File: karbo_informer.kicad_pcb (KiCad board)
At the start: 2 copper layers, 12 parts, among them IC1 MAX7219, IC2 MAX7219, P1 USB_OTG

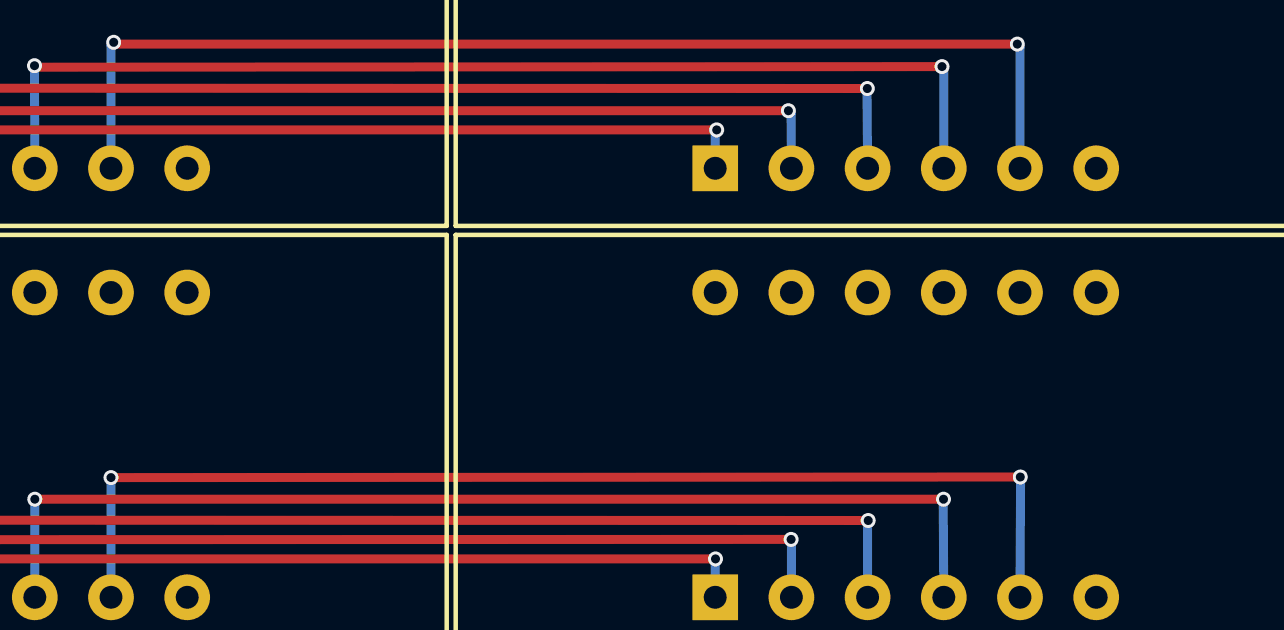
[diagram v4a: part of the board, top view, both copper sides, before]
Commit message: Wire for segments B in the sell line (D2 to D4)
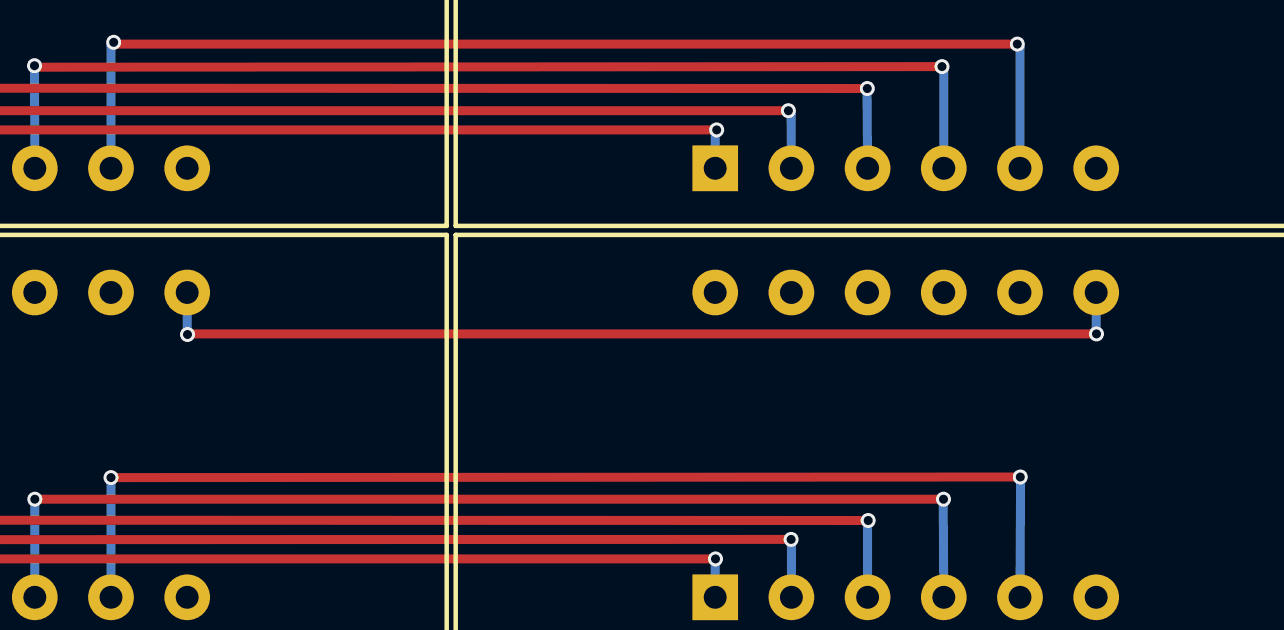
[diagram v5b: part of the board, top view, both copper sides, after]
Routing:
- net /S_SEG_B: track 0.00 -> 33.0 mm, vias 0 -> 2
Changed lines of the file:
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@@
   (general
     (links 69)
-    (no_connects 56)
+    (no_connects 55)
     (area 0 0 0 0)
     (thickness 1.6)
     (drawings 0)
-    (tracks 90)
+    (tracks 95)
     (zones 0)
     (modules 12)
@@
   (segment (start 44.62 44.29) (end 74.92 44.27) (width 0.3) (layer F.Cu) (net 17))
   (via (at 44.61 44.29) (size 0.5) (drill 0.3) (layers F.Cu B.Cu) (net 17))
+  (segment (start 47.15 38.12) (end 47.15 39.51) (width 0.3) (layer B.Cu) (net 24) (status 400000))
+  (segment (start 77.45 39.49) (end 77.45 38.12) (width 0.3) (layer B.Cu) (net 24) (status 800000))
+  (via (at 77.46 39.5) (size 0.5) (drill 0.3) (layers F.Cu B.Cu) (net 24))
+  (segment (start 47.18 39.5) (end 77.46 39.5) (width 0.3) (layer F.Cu) (net 24))
+  (via (at 47.16 39.52) (size 0.5) (drill 0.3) (layers F.Cu B.Cu) (net 24))
 )

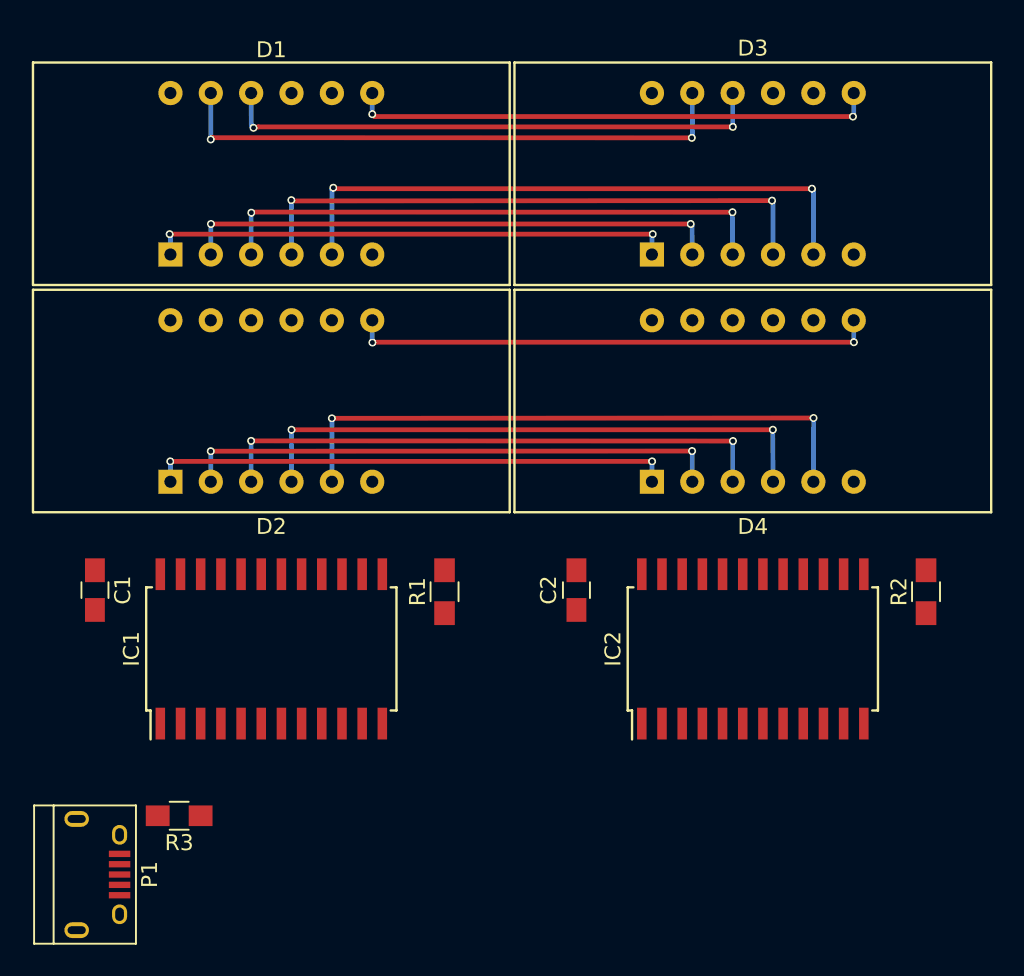
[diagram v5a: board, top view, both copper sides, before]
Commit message: Wire for DIG0 and other in the buy line
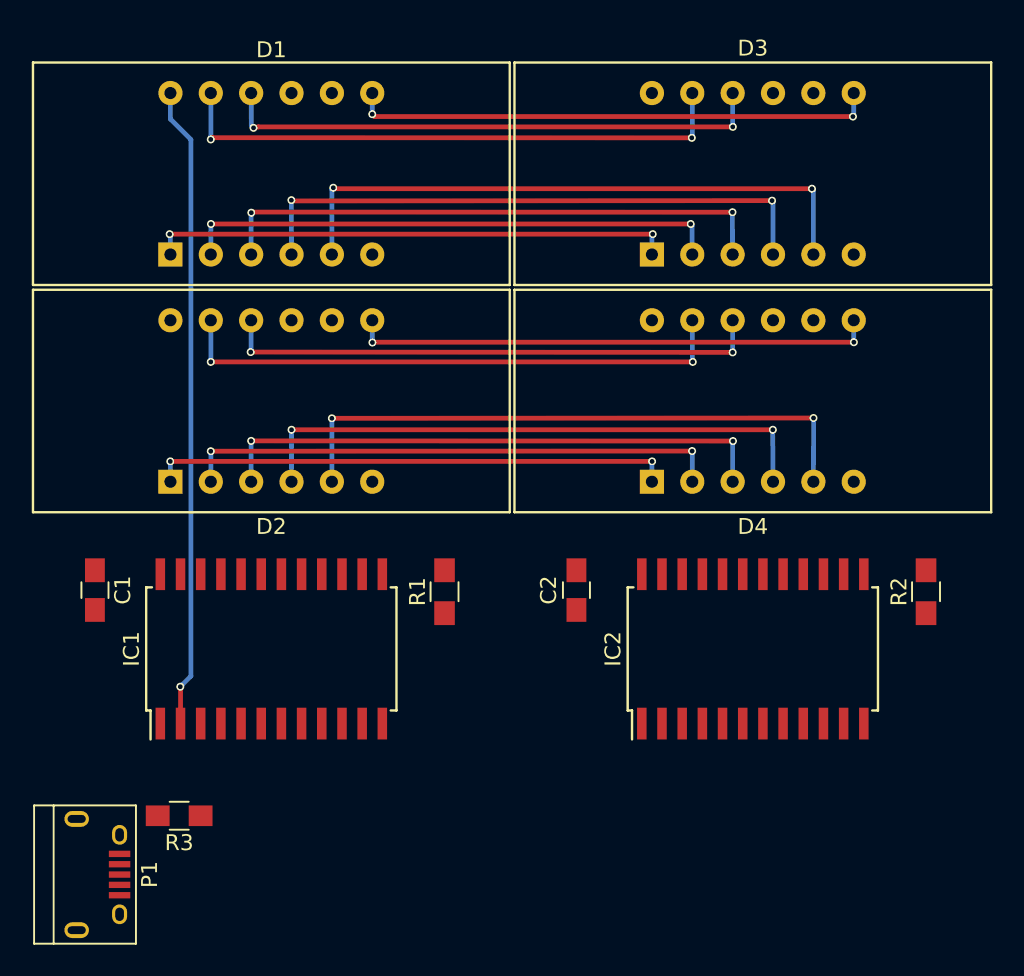
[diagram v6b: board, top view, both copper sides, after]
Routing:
- net /B_DIG_0: track 0.00 -> 40.5 mm, vias 0 -> 1
- net /S_SEG_A: track 0.00 -> 35.6 mm, vias 0 -> 2
- net /S_SEG_F: track 0.00 -> 34.3 mm, vias 0 -> 2
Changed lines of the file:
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@@
   (general
     (links 69)
-    (no_connects 55)
+    (no_connects 52)
     (area 0 0 0 0)
     (thickness 1.6)
     (drawings 0)
-    (tracks 95)
+    (tracks 112)
     (zones 0)
     (modules 12)
@@
   (segment (start 36.99 26.74) (end 37.1 26.63) (width 0.3) (layer F.Cu) (net 8))
   (via (at 36.99 26.74) (size 0.5) (drill 0.3) (layers F.Cu B.Cu) (net 8))
+  (segment (start 35.085 61.195) (end 35.085 63.5) (width 0.3) (layer F.Cu) (net 9))
+  (segment (start 35.07 61.18) (end 35.085 61.195) (width 0.3) (layer F.Cu) (net 9))
+  (via (at 35.07 61.18) (size 0.5) (drill 0.3) (layers F.Cu B.Cu) (net 9))
+  (segment (start 35.74 60.51) (end 35.07 61.18) (width 0.3) (layer B.Cu) (net 9))
+  (segment (start 35.74 26.75) (end 35.74 60.51) (width 0.3) (layer B.Cu) (net 9))
+  (segment (start 34.45 25.46) (end 35.74 26.75) (width 0.3) (layer B.Cu) (net 9))
+  (segment (start 34.45 23.82) (end 34.45 25.46) (width 0.3) (layer B.Cu) (net 9))
   (via (at 77.4 25.3) (size 0.5) (drill 0.3) (layers F.Cu B.Cu) (net 12))
   (segment (start 77.4 25.3) (end 77.45 25.3) (width 0.3) (layer B.Cu) (net 12))
@@
   (via (at 69.85 45.72) (size 0.5) (drill 0.3) (layers F.Cu B.Cu) (net 14))
   (segment (start 69.85 45.72) (end 69.83 45.74) (width 0.3) (layer B.Cu) (net 14))
-  (segment (start 69.83 48.28) (end 69.83 45.74) (width 0.3) (layer B.Cu) (net 14) (status 400000))
+  (segment (start 69.83 48.28) (end 69.83 45.74) (width 0.3) (layer B.Cu) (net 14))
   (segment (start 39.53 45.71) (end 39.53 48.3) (width 0.3) (layer B.Cu) (net 14))
   (via (at 36.99 46.36) (size 0.5) (drill 0.3) (layers F.Cu B.Cu) (net 15))
   (via (at 67.28 46.35) (size 0.5) (drill 0.3) (layers F.Cu B.Cu) (net 15))
   (segment (start 67.28 46.35) (end 36.99 46.36) (width 0.3) (layer F.Cu) (net 15))
-  (segment (start 36.99 46.36) (end 36.99 48.28) (width 0.3) (layer B.Cu) (net 15) (status 800000))
+  (segment (start 36.99 46.36) (end 36.99 48.28) (width 0.3) (layer B.Cu) (net 15))
   (segment (start 67.29 46.36) (end 67.29 48.28) (width 0.3) (layer B.Cu) (net 15))
   (via (at 42.07 45.01) (size 0.5) (drill 0.3) (layers F.Cu B.Cu) (net 16))
-  (segment (start 42.07 48.28) (end 42.07 45.01) (width 0.3) (layer B.Cu) (net 16) (status 400000))
-  (segment (start 72.35 45.02) (end 72.37 48.28) (width 0.3) (layer B.Cu) (net 16) (status 800000))
+  (segment (start 42.07 48.28) (end 42.07 45.01) (width 0.3) (layer B.Cu) (net 16))
+  (segment (start 72.35 45.02) (end 72.37 48.28) (width 0.3) (layer B.Cu) (net 16))
   (via (at 72.36 45.01) (size 0.5) (drill 0.3) (layers F.Cu B.Cu) (net 16))
   (segment (start 42.07 45.01) (end 72.36 45.01) (width 0.3) (layer F.Cu) (net 16))
-  (segment (start 44.61 48.28) (end 44.61 44.29) (width 0.3) (layer B.Cu) (net 17) (status 400000))
-  (segment (start 74.93 44.28) (end 74.91 48.28) (width 0.3) (layer B.Cu) (net 17) (status 800000))
+  (segment (start 44.61 48.28) (end 44.61 44.29) (width 0.3) (layer B.Cu) (net 17))
+  (segment (start 74.93 44.28) (end 74.91 48.28) (width 0.3) (layer B.Cu) (net 17))
   (via (at 74.92 44.27) (size 0.5) (drill 0.3) (layers F.Cu B.Cu) (net 17))
   (segment (start 44.62 44.29) (end 74.92 44.27) (width 0.3) (layer F.Cu) (net 17))
   (via (at 44.61 44.29) (size 0.5) (drill 0.3) (layers F.Cu B.Cu) (net 17))
-  (segment (start 47.15 38.12) (end 47.15 39.51) (width 0.3) (layer B.Cu) (net 24) (status 400000))
-  (segment (start 77.45 39.49) (end 77.45 38.12) (width 0.3) (layer B.Cu) (net 24) (status 800000))
+  (via (at 39.5 40.12) (size 0.5) (drill 0.3) (layers F.Cu B.Cu) (net 19))
+  (segment (start 39.5 40.12) (end 69.83 40.14) (width 0.3) (layer F.Cu) (net 19))
+  (via (at 69.83 40.14) (size 0.5) (drill 0.3) (layers F.Cu B.Cu) (net 19))
+  (segment (start 69.83 38.12) (end 69.83 40.14) (width 0.3) (layer B.Cu) (net 19))
+  (segment (start 39.53 40.09) (end 39.53 38.12) (width 0.3) (layer B.Cu) (net 19))
+  (segment (start 36.99 40.74) (end 36.99 38.12) (width 0.3) (layer B.Cu) (net 20))
+  (via (at 36.99 40.74) (size 0.5) (drill 0.3) (layers F.Cu B.Cu) (net 20))
+  (segment (start 67.29 38.12) (end 67.3 40.72) (width 0.3) (layer B.Cu) (net 20))
+  (via (at 67.32 40.74) (size 0.5) (drill 0.3) (layers F.Cu B.Cu) (net 20))
+  (segment (start 36.99 40.74) (end 67.32 40.74) (width 0.3) (layer F.Cu) (net 20))
+  (segment (start 47.15 38.12) (end 47.15 39.51) (width 0.3) (layer B.Cu) (net 24))
+  (segment (start 77.45 39.49) (end 77.45 38.12) (width 0.3) (layer B.Cu) (net 24))
   (via (at 77.46 39.5) (size 0.5) (drill 0.3) (layers F.Cu B.Cu) (net 24))
   (segment (start 47.18 39.5) (end 77.46 39.5) (width 0.3) (layer F.Cu) (net 24))

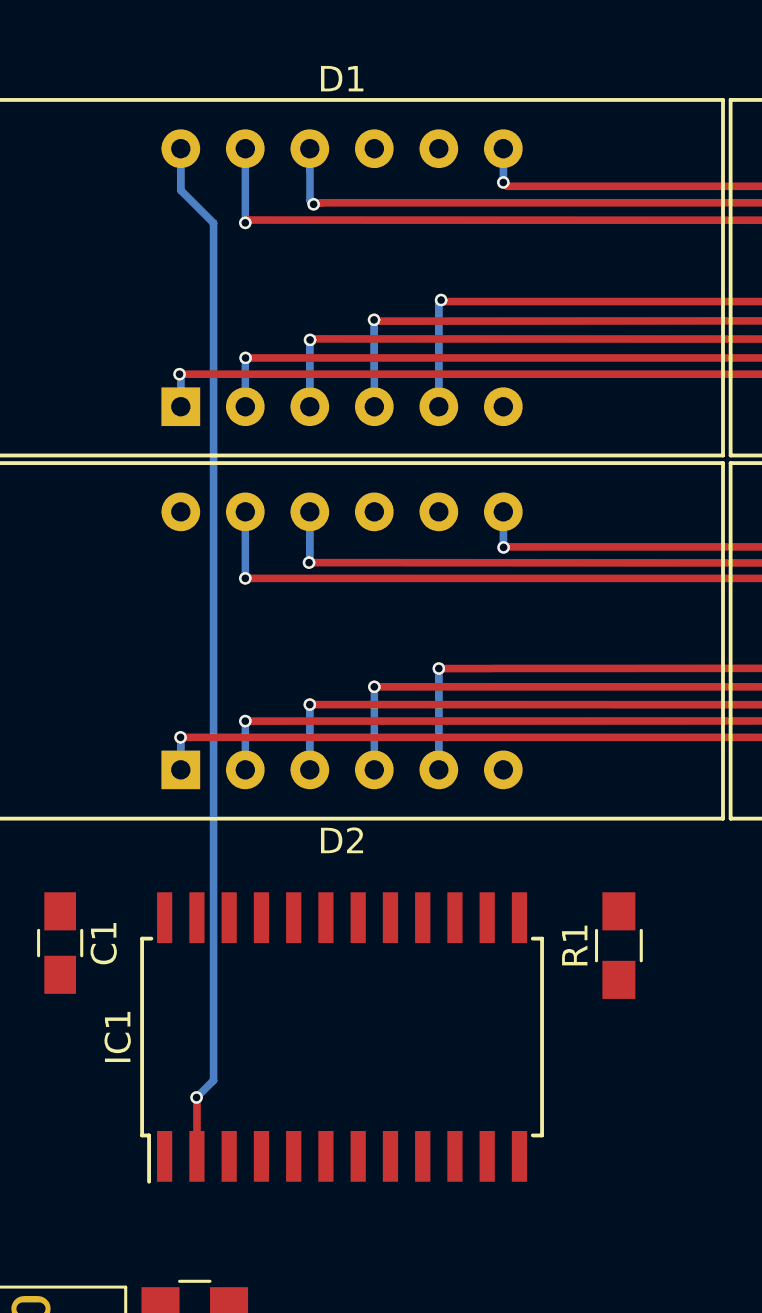
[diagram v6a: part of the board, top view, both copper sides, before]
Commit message: Wire for DIG2 to MAX7219 in the buy line
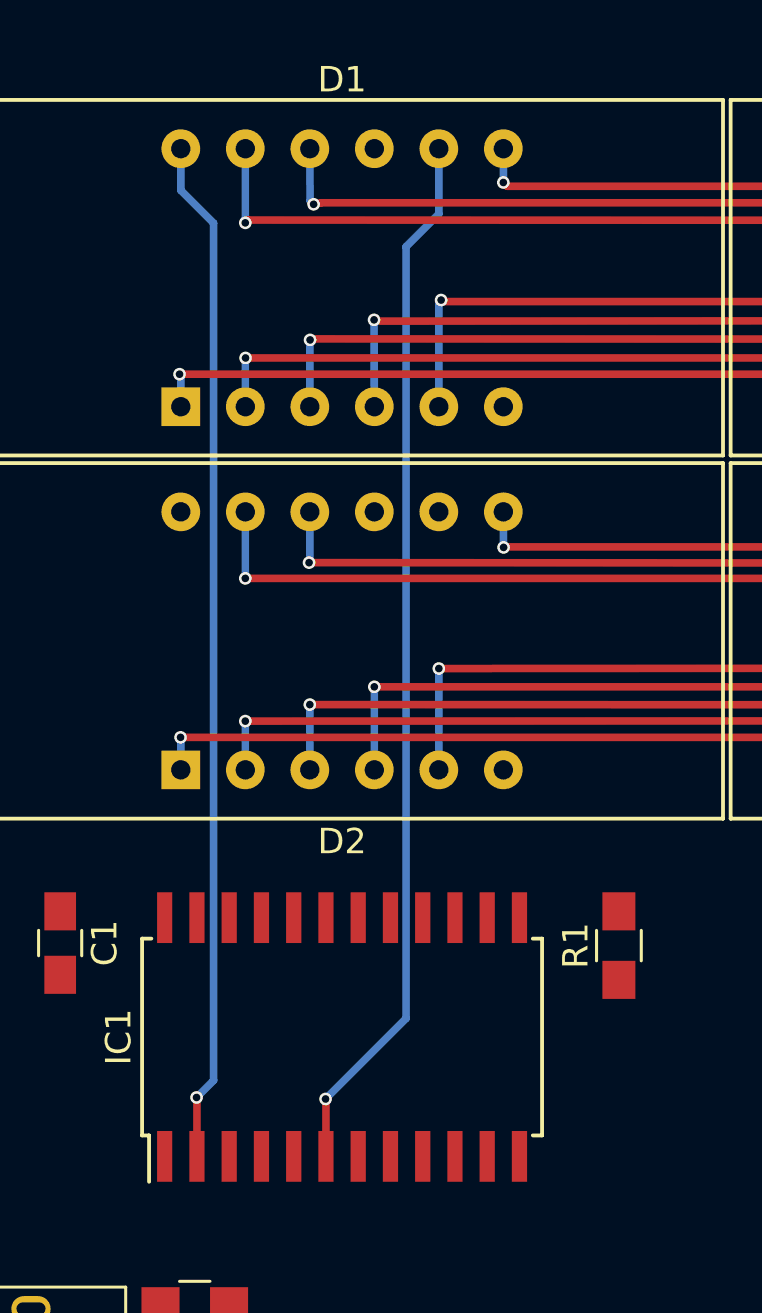
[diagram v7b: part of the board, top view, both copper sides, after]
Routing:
- net /B_DIG_2: track 0.00 -> 41.5 mm, vias 0 -> 1
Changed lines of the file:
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@@
   (general
     (links 69)
-    (no_connects 52)
+    (no_connects 51)
     (area 0 0 0 0)
     (thickness 1.6)
     (drawings 0)
-    (tracks 112)
+    (tracks 119)
     (zones 0)
     (modules 12)
@@
   (segment (start 34.45 25.46) (end 35.74 26.75) (width 0.3) (layer B.Cu) (net 9))
   (segment (start 34.45 23.82) (end 34.45 25.46) (width 0.3) (layer B.Cu) (net 9))
+  (segment (start 44.61 23.82) (end 44.61 26.39) (width 0.3) (layer B.Cu) (net 11) (status 400000))
+  (segment (start 40.165 61.255) (end 40.165 63.5) (width 0.3) (layer F.Cu) (net 11) (status 800000))
+  (segment (start 40.15 61.24) (end 40.165 61.255) (width 0.3) (layer F.Cu) (net 11))
+  (via (at 40.15 61.24) (size 0.5) (drill 0.3) (layers F.Cu B.Cu) (net 11))
+  (segment (start 43.32 58.07) (end 40.15 61.24) (width 0.3) (layer B.Cu) (net 11))
+  (segment (start 43.32 27.68) (end 43.32 58.07) (width 0.3) (layer B.Cu) (net 11))
+  (segment (start 44.61 26.39) (end 43.32 27.68) (width 0.3) (layer B.Cu) (net 11))
   (via (at 77.4 25.3) (size 0.5) (drill 0.3) (layers F.Cu B.Cu) (net 12))
   (segment (start 77.4 25.3) (end 77.45 25.3) (width 0.3) (layer B.Cu) (net 12))
